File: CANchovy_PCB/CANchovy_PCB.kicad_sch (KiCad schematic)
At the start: 77 parts, among them J1 USB_C_Receptacle_USB2.0, J2 KH-RJ45-56-8P8C-D, J3 KH-RJ45-56-8P8C-D, Q1 AO3401A, Q2 AO3401A, Q6 SS8050, SW1 BOOT, SW2 DSWB02LHGET, U1 STM32G431C8T6, U2 HT7533-1, U3 TJA1051T-3, U4 ADuM1201BR, U5 TPD4E1U06DCKR, U6 B0505S-1WR3, U7 TPD4E1U06DCKR, U8 NC7SZ125P5X

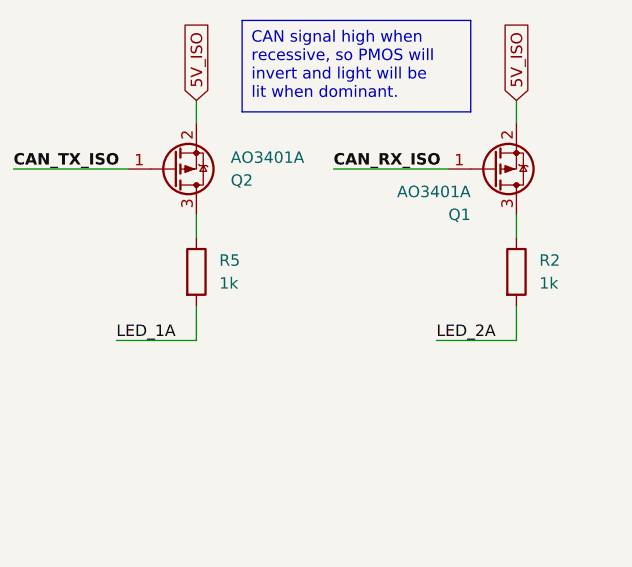
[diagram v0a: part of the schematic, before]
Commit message: Revision B release.
Changes:
- Silkscreen numbering corrected for RJ45 numberings.
- RJ45 LEDs for RX/TX now ~twice the current.
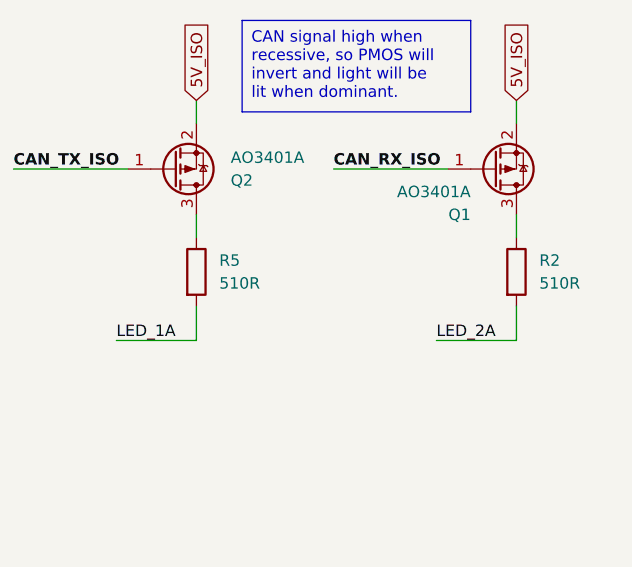
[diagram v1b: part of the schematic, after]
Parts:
- R2, R5: value 1k -> 510R; LCSC Part # C21190 -> C23193; Manufacturer Part # 0603WAF1001T5E -> 0603WAF5100T5E
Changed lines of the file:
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@@
   (title_block
     (title "CANchovy")
-    (date "2023-10-31")
-    (rev "A")
+    (date "2023-11-16")
+    (rev "B")
     (company "N/A")
     (comment 1 "MKS CANable V2 based")
@@
       (effects (font (size 1.27 1.27)) (justify left))
     )
-    (property "Value" "1k" (at 400.05 241.3 0)
+    (property "Value" "510R" (at 400.05 241.3 0)
       (effects (font (size 1.27 1.27)) (justify left))
     )
@@
       (effects (font (size 1.27 1.27)) hide)
     )
-    (property "Datasheet" "https://datasheet.lcsc.com/lcsc/2206010130_UNI-ROYAL-Uniroyal-Elec-0603WAF1001T5E_C21190.pdf" (at 397.51 240.03 0)
+    (property "Datasheet" "https://datasheet.lcsc.com/lcsc/2206010116_UNI-ROYAL-Uniroyal-Elec-0603WAF5100T5E_C23193.pdf" (at 397.51 240.03 0)
       (effects (font (size 1.27 1.27)) hide)
     )
@@
       (effects (font (size 1.27 1.27)) hide)
     )
-    (property "Manufacturer Part #" "0603WAF1001T5E" (at 397.51 240.03 0)
+    (property "Manufacturer Part #" "0603WAF5100T5E" (at 397.51 240.03 0)
       (effects (font (size 1.27 1.27)) hide)
     )
-    (property "LCSC Part #" "C21190" (at 397.51 240.03 0)
+    (property "LCSC Part #" "C23193" (at 397.51 240.03 0)
       (effects (font (size 1.27 1.27)) hide)
     )
@@
       (effects (font (size 1.27 1.27)) (justify left))
     )
-    (property "Value" "1k" (at 364.49 241.3 0)
+    (property "Value" "510R" (at 364.49 241.3 0)
       (effects (font (size 1.27 1.27)) (justify left))
     )
@@
       (effects (font (size 1.27 1.27)) hide)
     )
-    (property "Datasheet" "https://datasheet.lcsc.com/lcsc/2206010130_UNI-ROYAL-Uniroyal-Elec-0603WAF1001T5E_C21190.pdf" (at 361.95 240.03 0)
+    (property "Datasheet" "https://datasheet.lcsc.com/lcsc/2206010116_UNI-ROYAL-Uniroyal-Elec-0603WAF5100T5E_C23193.pdf" (at 361.95 240.03 0)
       (effects (font (size 1.27 1.27)) hide)
     )
@@
       (effects (font (size 1.27 1.27)) hide)
     )
-    (property "Manufacturer Part #" "0603WAF1001T5E" (at 361.95 240.03 0)
+    (property "Manufacturer Part #" "0603WAF5100T5E" (at 361.95 240.03 0)
       (effects (font (size 1.27 1.27)) hide)
     )
-    (property "LCSC Part #" "C21190" (at 361.95 240.03 0)
+    (property "LCSC Part #" "C23193" (at 361.95 240.03 0)
       (effects (font (size 1.27 1.27)) hide)
     )

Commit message: Release V1.0
Green LED D3 changed to C965804.
Blue LED D2 changed to C965807.
README edits.
Design files updated to KiCAD V8 format.
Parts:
- D2: LCSC Part # C72041 -> C965807; Manufacturer Everlight Elec -> XINGLIGHT; Manufacturer Part # 19-217/BHC-ZL1M2RY/3T -> XL-1608UBC-04
- D3: LCSC Part # C72043 -> C965804; Manufacturer Everlight Elec -> XINGLIGHT; Manufacturer Part # 19-217/GHC-YR1S2/3T -> XL-1608UGC-04
